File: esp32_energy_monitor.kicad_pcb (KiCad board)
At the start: 4 copper layers, 54 x 38 mm, 54 parts, among them IC1 TPS63031DSKT, IC2 CP2102N-A01-GQFN28, J1 USB_OTG, J2 Conn_01x02, J3 Conn_01x02, J4 Conn_01x02, J5 Conn_01x16, J6 Conn_01x16, Q1 SS8050-G, Q2 SS8050-G, SW1 SW_Push, SW2 SW_Push

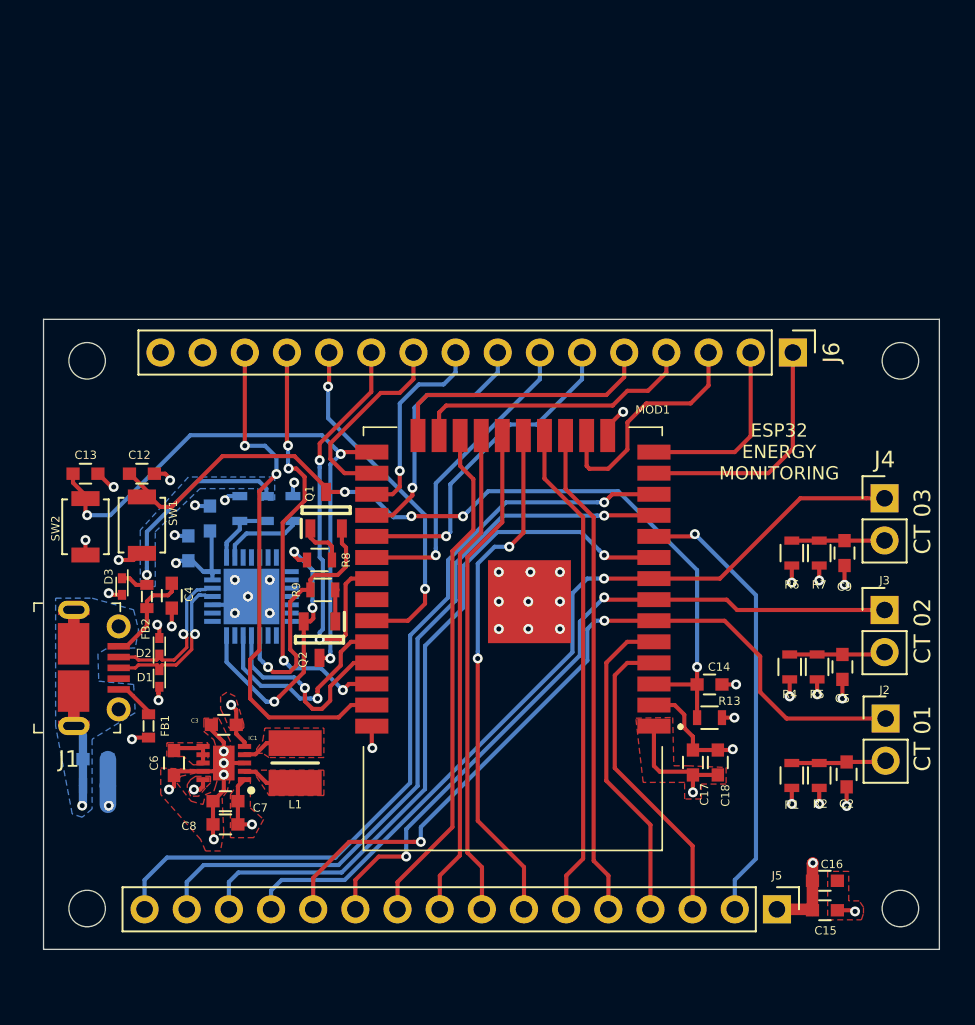
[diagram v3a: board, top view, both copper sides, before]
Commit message: Improved the layout of the J5 and J6 to expose all the pins of the ESP32 module.
Added the Final version of Bill of Materials (BoM).

Added all the gerber files.
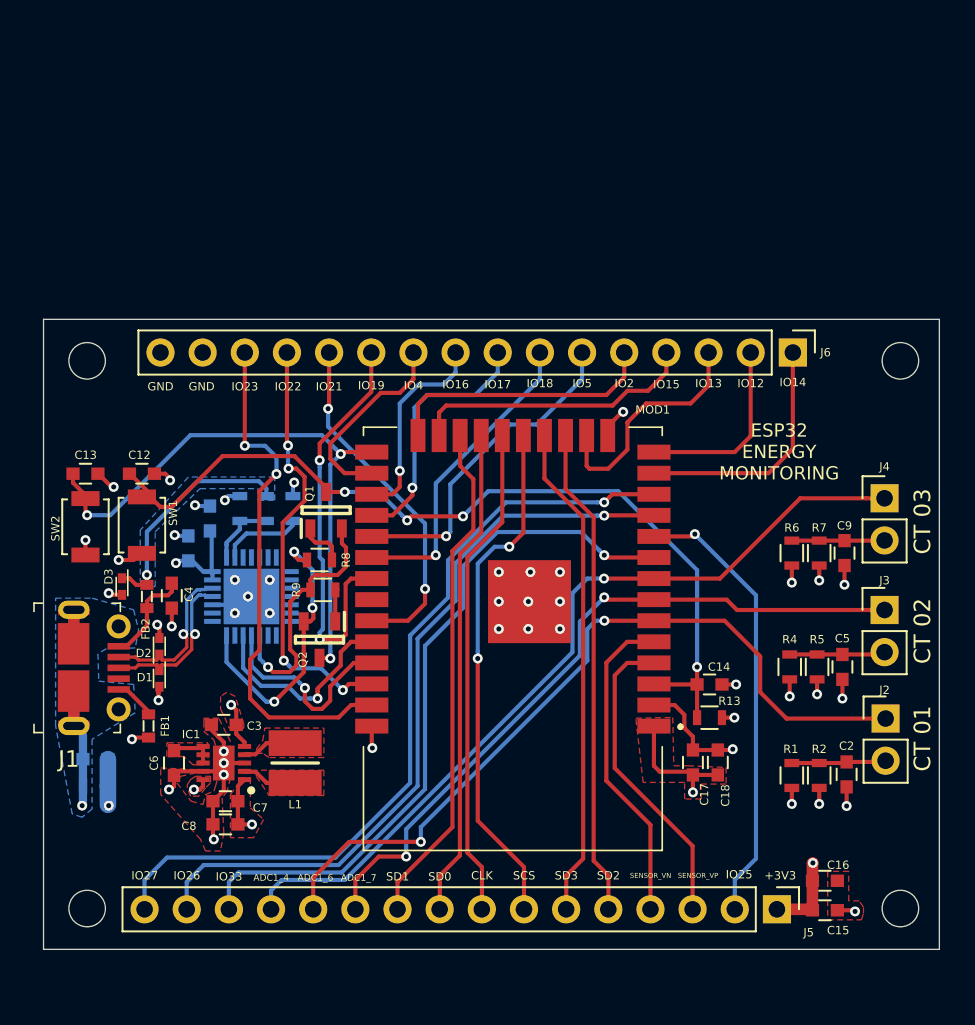
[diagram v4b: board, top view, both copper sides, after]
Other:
- board text added: "+3V3"
- board text added: "ADC1_4"
- board text added: "ADC1_6"
- board text added: "ADC1_7"
- board text added: "CLK"
- board text added: "GND"
- board text added: "IO12"
- board text added: "IO13"
- board text added: "IO14"
- board text added: "IO15"
- board text added: "IO16"
- board text added: "IO17"
- board text added: "IO18"
- board text added: "IO19"
- board text added: "IO2"
- board text added: "IO21"
- board text added: "IO22"
- board text added: "IO23"
- board text added: "IO25"
- board text added: "IO26"
- board text added: "IO27"
- board text added: "IO33"
- board text added: "IO4"
- board text added: "IO5"
- board text added: "SCS"
- board text added: "SD0"
- board text added: "SD1"
- board text added: "SD2"
- board text added: "SD3"
- board text added: "SENSOR_VN"
- board text added: "SENSOR_VP"
